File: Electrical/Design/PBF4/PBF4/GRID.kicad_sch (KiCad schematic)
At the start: 9 parts, among them J501 AFB10-S08LCA-00, J502 AFB10-S08LCA-00, J503 AFB10-S08LCA-00, J504 AFB10-S08LCA-00, J505 AFB10-S08LCA-00, J506 AFB10-S08LCA-00, J507 AFB10-S08LCA-00, J508 AFB10-S08LCA-00, M501 (NF)

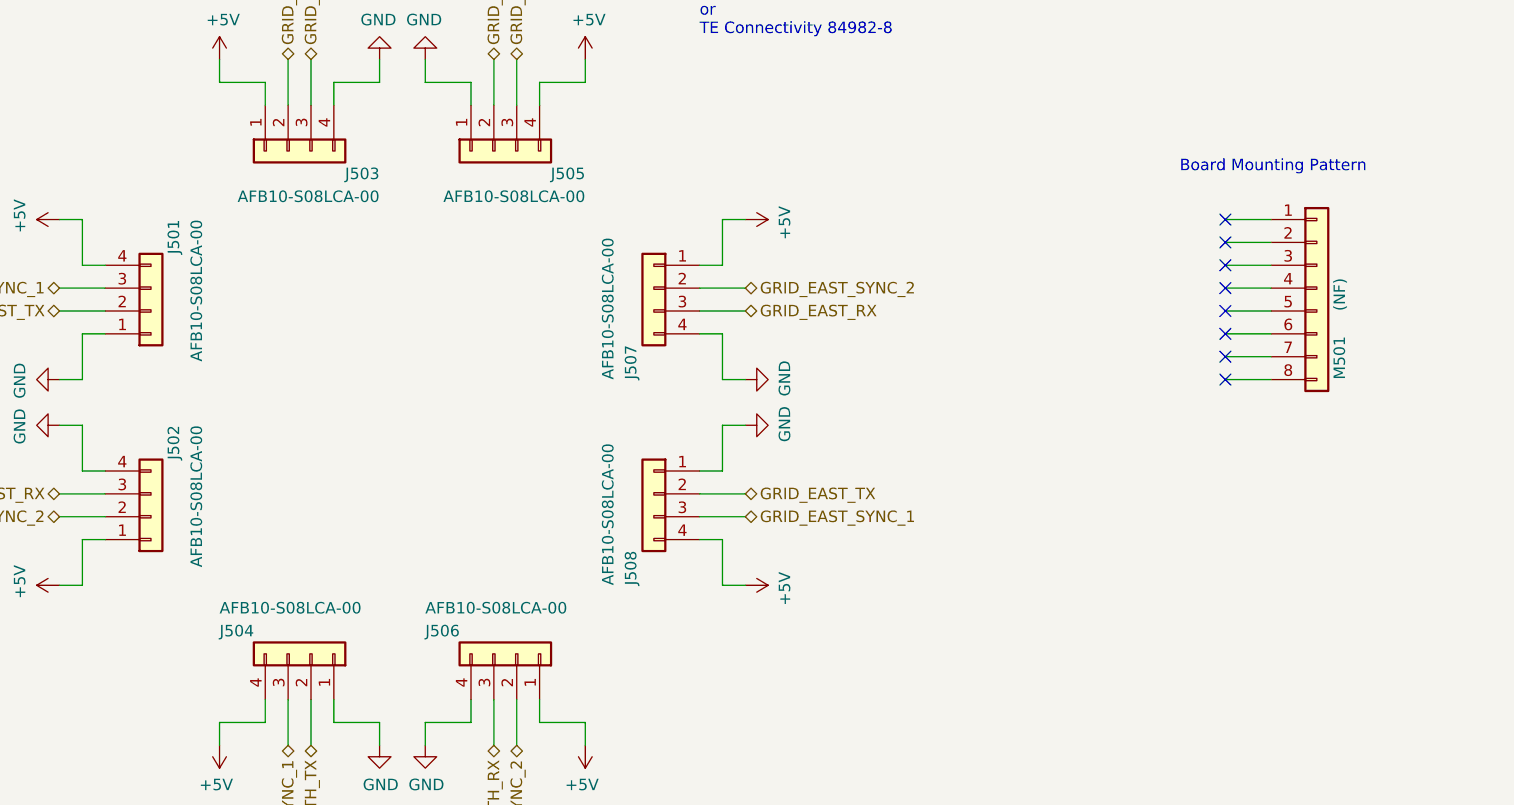
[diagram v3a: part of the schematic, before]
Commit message: SUKU testpoints added
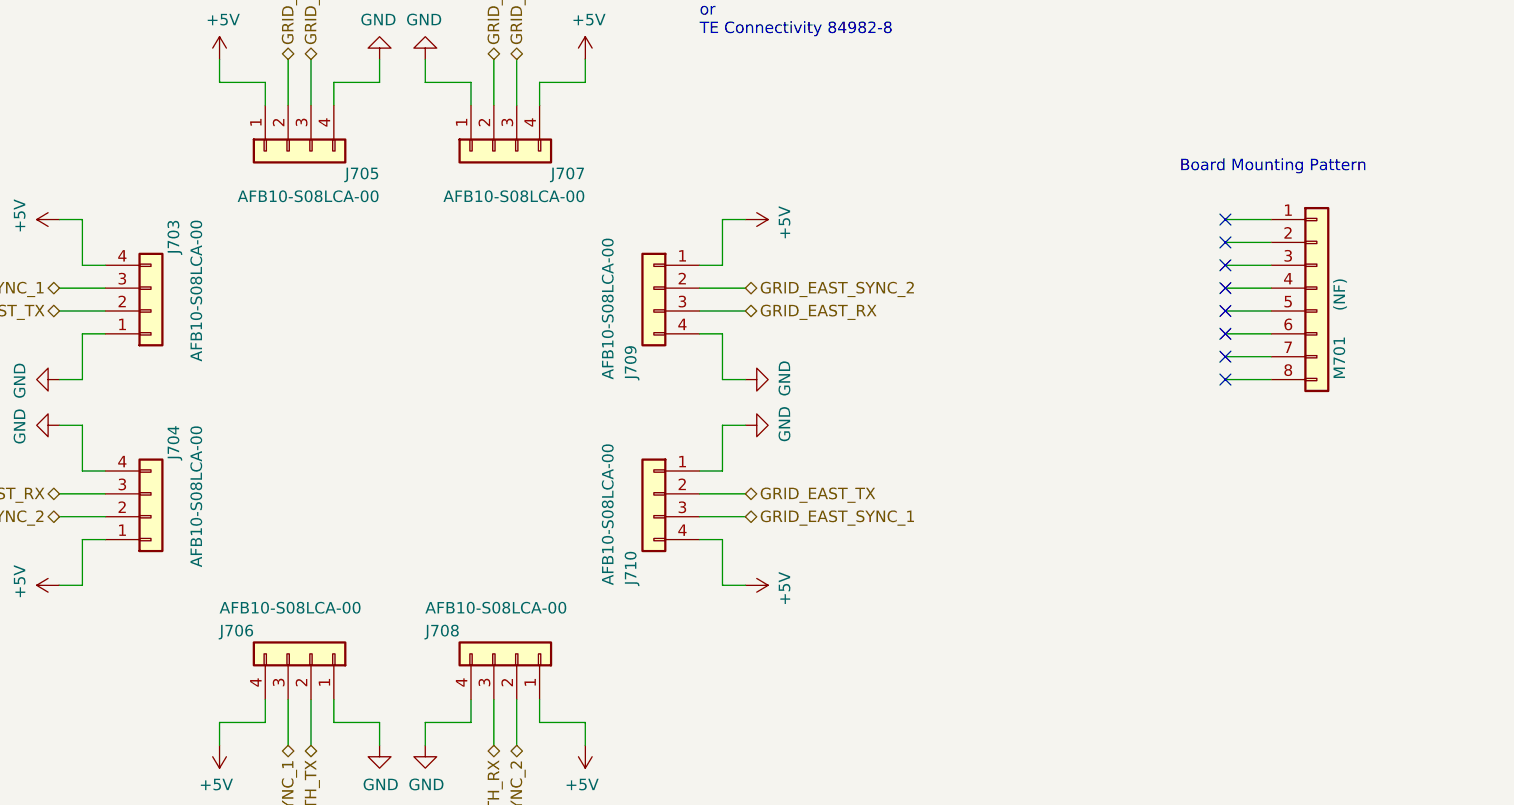
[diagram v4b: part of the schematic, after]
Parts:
- renumbered J501 to J703, J502 to J704, J503 to J705, J504 to J706, J505 to J707, J506 to J708, J507 to J709, J508 to J710, M501 to M701
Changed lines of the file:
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@@
   (symbol (lib_id "Connector_Generic:Conn_01x04") (at 48.26 66.04 0) (mirror x) (unit 1)
     (in_bom no) (on_board yes)
-    (property "Reference" "J501" (id 0) (at 50.8 55.88 90)
+    (property "Reference" "J703" (id 0) (at 50.8 55.88 90)
       (effects (font (size 1.27 1.27)) (justify left))
     )
@@
   (symbol (lib_id "Connector_Generic:Conn_01x04") (at 48.26 88.9 0) (mirror x) (unit 1)
     (in_bom no) (on_board yes)
-    (property "Reference" "J502" (id 0) (at 50.8 78.74 90)
+    (property "Reference" "J704" (id 0) (at 50.8 78.74 90)
       (effects (font (size 1.27 1.27)) (justify left))
     )
@@
   (symbol (lib_id "power:+5V") (at 38.1 55.88 90) (unit 1)
     (in_bom yes) (on_board yes)
-    (property "Reference" "#PWR0502" (id 0) (at 41.91 55.88 0)
+    (property "Reference" "#PWR0847" (id 0) (at 41.91 55.88 0)
       (effects (font (size 1.27 1.27)) hide)
     )
@@
   (symbol (lib_id "power:GND") (at 38.1 73.66 270) (unit 1)
     (in_bom yes) (on_board yes)
-    (property "Reference" "#PWR0504" (id 0) (at 31.75 73.66 0)
+    (property "Reference" "#PWR0848" (id 0) (at 31.75 73.66 0)
       (effects (font (size 1.27 1.27)) hide)
     )
@@
   (symbol (lib_id "power:GND") (at 38.1 78.74 270) (unit 1)
     (in_bom yes) (on_board yes)
-    (property "Reference" "#PWR0501" (id 0) (at 31.75 78.74 0)
+    (property "Reference" "#PWR0849" (id 0) (at 31.75 78.74 0)
       (effects (font (size 1.27 1.27)) hide)
     )
@@
   (symbol (lib_id "power:+5V") (at 38.1 96.52 90) (unit 1)
     (in_bom yes) (on_board yes)
-    (property "Reference" "#PWR0503" (id 0) (at 41.91 96.52 0)
+    (property "Reference" "#PWR0850" (id 0) (at 41.91 96.52 0)
       (effects (font (size 1.27 1.27)) hide)
     )
@@
   (symbol (lib_id "Connector_Generic:Conn_01x04") (at 86.36 48.26 90) (mirror x) (unit 1)
     (in_bom no) (on_board yes)
-    (property "Reference" "J505" (id 0) (at 96.52 50.8 90)
+    (property "Reference" "J707" (id 0) (at 96.52 50.8 90)
       (effects (font (size 1.27 1.27)) (justify left))
     )
@@
   (symbol (lib_id "Connector_Generic:Conn_01x04") (at 63.5 48.26 90) (mirror x) (unit 1)
     (in_bom no) (on_board yes)
-    (property "Reference" "J503" (id 0) (at 73.66 50.8 90)
+    (property "Reference" "J705" (id 0) (at 73.66 50.8 90)
       (effects (font (size 1.27 1.27)) (justify left))
     )
@@
   (symbol (lib_id "Connector_Generic:Conn_01x04") (at 104.14 86.36 0) (mirror y) (unit 1)
     (in_bom no) (on_board yes)
-    (property "Reference" "J508" (id 0) (at 101.6 96.52 90)
+    (property "Reference" "J710" (id 0) (at 101.6 96.52 90)
       (effects (font (size 1.27 1.27)) (justify left))
     )
@@
   (symbol (lib_id "Connector_Generic:Conn_01x04") (at 104.14 63.5 0) (mirror y) (unit 1)
     (in_bom no) (on_board yes)
-    (property "Reference" "J507" (id 0) (at 101.6 73.66 90)
+    (property "Reference" "J709" (id 0) (at 101.6 73.66 90)
       (effects (font (size 1.27 1.27)) (justify left))
     )
@@
   (symbol (lib_id "Connector_Generic:Conn_01x04") (at 66.04 104.14 270) (mirror x) (unit 1)
     (in_bom no) (on_board yes)
-    (property "Reference" "J504" (id 0) (at 55.88 101.6 90)
+    (property "Reference" "J706" (id 0) (at 55.88 101.6 90)
       (effects (font (size 1.27 1.27)) (justify left))
     )
@@
   (symbol (lib_id "Connector_Generic:Conn_01x04") (at 88.9 104.14 270) (mirror x) (unit 1)
     (in_bom no) (on_board yes)
-    (property "Reference" "J506" (id 0) (at 78.74 101.6 90)
+    (property "Reference" "J708" (id 0) (at 78.74 101.6 90)
       (effects (font (size 1.27 1.27)) (justify left))
     )
@@
   (symbol (lib_id "Connector_Generic:Conn_01x08") (at 177.8 63.5 0) (unit 1)
     (in_bom yes) (on_board yes)
-    (property "Reference" "M501" (id 0) (at 180.34 73.66 90)
+    (property "Reference" "M701" (id 0) (at 180.34 73.66 90)
       (effects (font (size 1.27 1.27)) (justify left))
     )
@@
   (symbol (lib_id "power:+5V") (at 96.52 114.3 180) (unit 1)
     (in_bom yes) (on_board yes)
-    (property "Reference" "#PWR0158" (id 0) (at 96.52 110.49 0)
+    (property "Reference" "#PWR0858" (id 0) (at 96.52 110.49 0)
       (effects (font (size 1.27 1.27)) hide)
     )
@@
   (symbol (lib_id "power:+5V") (at 114.3 55.88 270) (unit 1)
     (in_bom yes) (on_board yes)
-    (property "Reference" "#PWR0167" (id 0) (at 110.49 55.88 0)
+    (property "Reference" "#PWR0859" (id 0) (at 110.49 55.88 0)
       (effects (font (size 1.27 1.27)) hide)
     )
@@
   (symbol (lib_id "power:+5V") (at 114.3 96.52 270) (unit 1)
     (in_bom yes) (on_board yes)
-    (property "Reference" "#PWR0166" (id 0) (at 110.49 96.52 0)
+    (property "Reference" "#PWR0862" (id 0) (at 110.49 96.52 0)
       (effects (font (size 1.27 1.27)) hide)
     )
@@
   (symbol (lib_id "power:+5V") (at 96.52 38.1 0) (unit 1)
     (in_bom yes) (on_board yes)
-    (property "Reference" "#PWR0156" (id 0) (at 96.52 41.91 0)
+    (property "Reference" "#PWR0857" (id 0) (at 96.52 41.91 0)
       (effects (font (size 1.27 1.27)) hide)
     )
@@
   (symbol (lib_id "power:GND") (at 114.3 78.74 90) (unit 1)
     (in_bom yes) (on_board yes)
-    (property "Reference" "#PWR0165" (id 0) (at 120.65 78.74 0)
+    (property "Reference" "#PWR0861" (id 0) (at 120.65 78.74 0)
       (effects (font (size 1.27 1.27)) hide)
     )
@@
   (symbol (lib_id "power:GND") (at 78.74 38.1 180) (unit 1)
     (in_bom yes) (on_board yes)
-    (property "Reference" "#PWR0110" (id 0) (at 78.74 31.75 0)
+    (property "Reference" "#PWR0855" (id 0) (at 78.74 31.75 0)
       (effects (font (size 1.27 1.27)) hide)
     )
@@
   (symbol (lib_id "power:GND") (at 73.66 38.1 180) (unit 1)
     (in_bom yes) (on_board yes)
-    (property "Reference" "#PWR0111" (id 0) (at 73.66 31.75 0)
+    (property "Reference" "#PWR0853" (id 0) (at 73.66 31.75 0)
       (effects (font (size 1.27 1.27)) hide)
     )
@@
   (symbol (lib_id "power:GND") (at 73.66 114.3 0) (unit 1)
     (in_bom yes) (on_board yes)
-    (property "Reference" "#PWR0162" (id 0) (at 73.66 120.65 0)
+    (property "Reference" "#PWR0854" (id 0) (at 73.66 120.65 0)
       (effects (font (size 1.27 1.27)) hide)
     )
@@
   (symbol (lib_id "power:+5V") (at 55.88 38.1 0) (unit 1)
     (in_bom yes) (on_board yes)
-    (property "Reference" "#PWR0157" (id 0) (at 55.88 41.91 0)
+    (property "Reference" "#PWR0851" (id 0) (at 55.88 41.91 0)
       (effects (font (size 1.27 1.27)) hide)
     )
@@
   (symbol (lib_id "power:GND") (at 78.74 114.3 0) (unit 1)
     (in_bom yes) (on_board yes)
-    (property "Reference" "#PWR0161" (id 0) (at 78.74 120.65 0)
+    (property "Reference" "#PWR0856" (id 0) (at 78.74 120.65 0)
       (effects (font (size 1.27 1.27)) hide)
     )
@@
   (symbol (lib_id "power:GND") (at 114.3 73.66 90) (unit 1)
     (in_bom yes) (on_board yes)
-    (property "Reference" "#PWR0163" (id 0) (at 120.65 73.66 0)
+    (property "Reference" "#PWR0860" (id 0) (at 120.65 73.66 0)
       (effects (font (size 1.27 1.27)) hide)
     )
@@
   (symbol (lib_id "power:+5V") (at 55.88 114.3 180) (unit 1)
     (in_bom yes) (on_board yes)
-    (property "Reference" "#PWR0159" (id 0) (at 55.88 110.49 0)
-      (effects (font (size 1.27 1.27)) hide)
-    )
+    (property "Reference" "#PWR0852" (id 0) (at 55.88 110.49 0)
+      (effects (font (size 1.27 1.27)) hide)
+    )
